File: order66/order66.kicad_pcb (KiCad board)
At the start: 2 copper layers, 232.6 x 124.3 mm, 144 parts, among them J1 NICEVIEW, J2 Pouch Battery Connector, SW1 AUX1, SW10 A, SW11 Z, SW12 AUX7, SW13 RST, SW14 2, SW15 W, SW16 S, SW17 X, SW18 LALT, SW19 ON/OFF, SW2 ESC, SW20 3, SW21 E, SW22 D, SW23 C, SW24 GUI, SW25 AUX5, SW26 4, SW27 R, SW28 F, SW29 V, SW3 TAB, SW30 RAISE, SW31 AUX4, SW32 5, SW33 T, SW34 G, SW35 B, SW36 AUX3, SW37 AUX2, SW38 6, SW39 Y, SW4 CAPSLCK, SW40 H, SW41 N, SW42 RSPACE, SW44 7, SW45 U, SW46 J, SW47 M, SW48 LOWER, SW5 LSHIFT, SW50 8, SW51 I, SW52 K, SW53 ,<, SW54 LEFT, SW56 9, SW57 O, SW58 L, SW59 .>, SW6 LCTRL, SW60 DOWN, SW62 0, SW63 P, SW64 ;:, SW65 /?, SW66 UP, SW67 AUX6, SW68 BACKSPACE, SW69 BACKSLACH, SW7 LSPACE, SW70 ENTER, SW71 RSHIFT, SW72 RIGHT, SW8 1, SW9 Q, U1 NiceNano

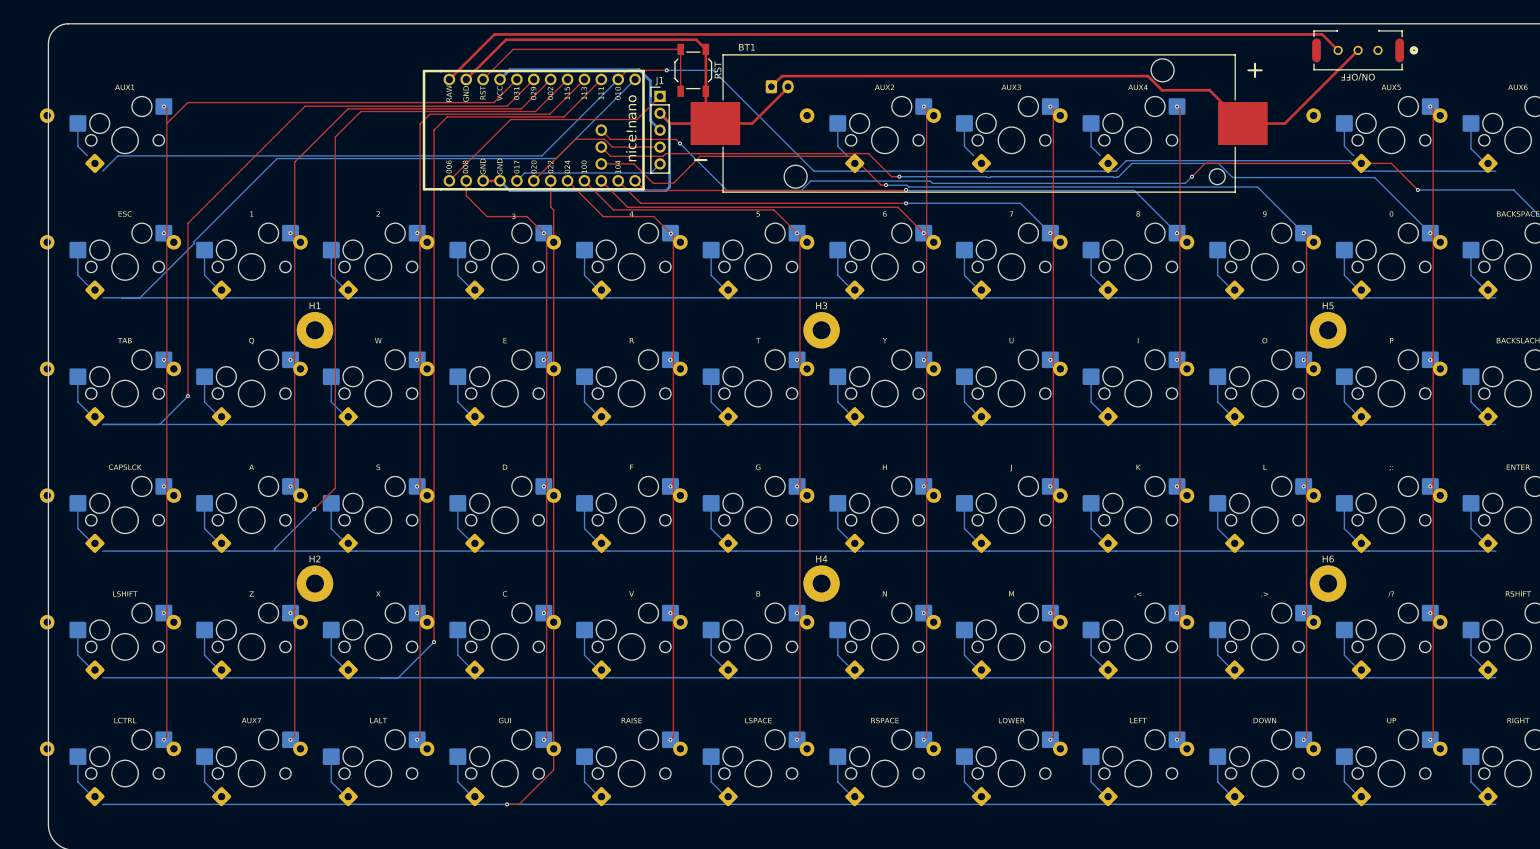
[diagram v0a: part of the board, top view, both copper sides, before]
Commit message: removing unused library files
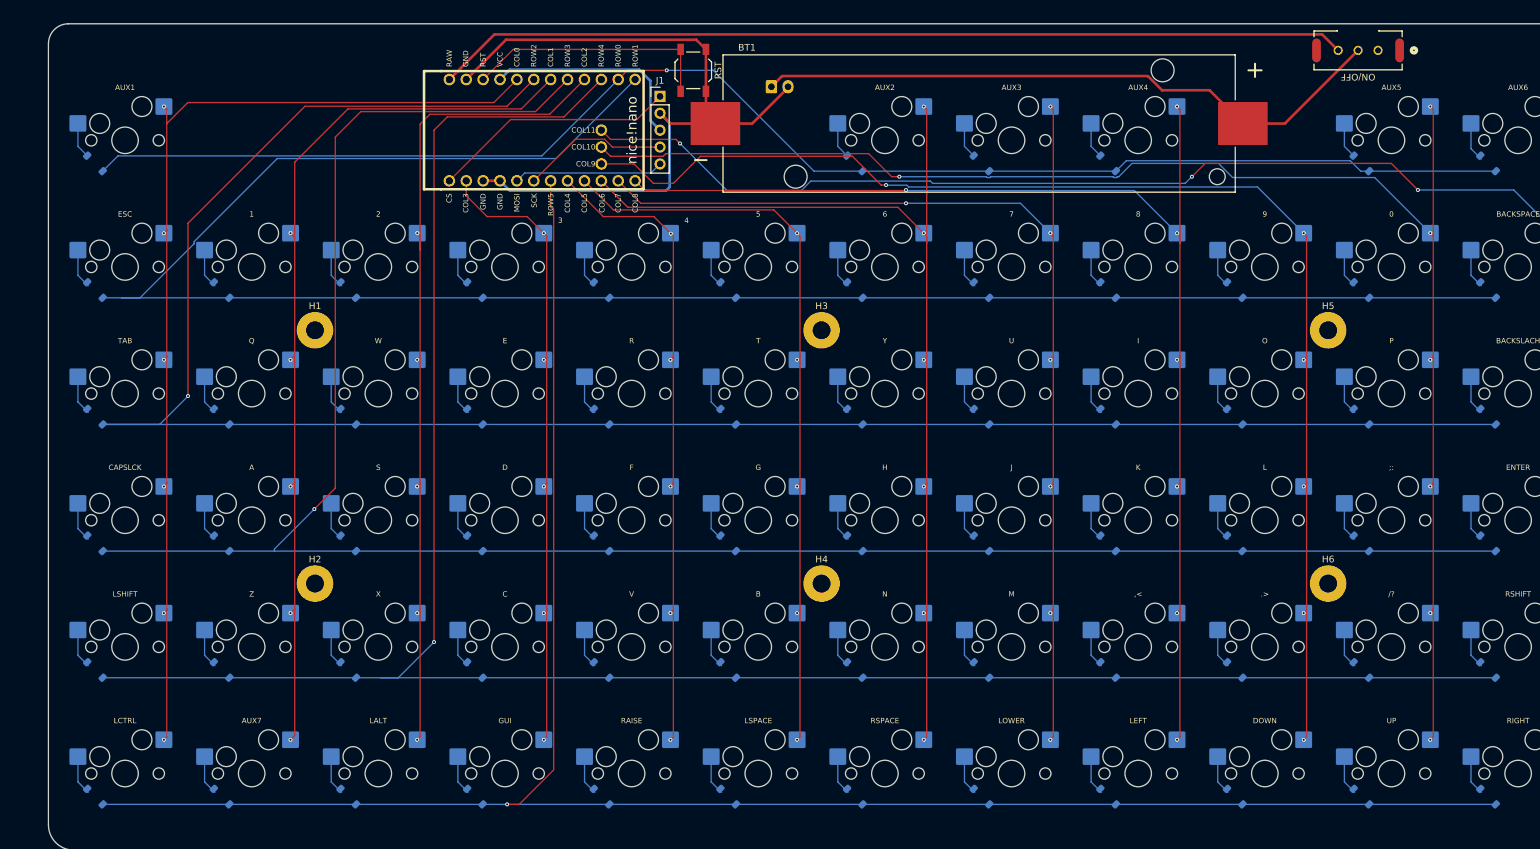
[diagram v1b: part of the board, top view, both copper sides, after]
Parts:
- D1, D10, D11, D12, D13, D14, D15, D16, D17, D18, D19, D2, D20, D21, D22, D23, D24, D25, D26, D27, D28, D29, D3, D30, D31, D32, D33, D34, D35, D38, D39, D4, D40, D41, D42, D44, D45, D46, D47, D48, D5, D50, D51, D52, D53, D54, D56, D57, D58, D59, D6, D60, D62, D63, D64, D65, D66, D67, D68, D69, D7, D70, D71, D72, D8, D9: footprint Diode_THT:D_DO-41_SOD81_P10.16mm_Horizontal -> Diode_SMD:D_SOD-123

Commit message: moved to more through hole components and rerouted traces
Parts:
- BT1: footprint 1042:BAT_1042 -> 1043P:BAT_1043P
- D1, D10, D11, D12, D13, D14, D15, D16, D17, D18, D19, D2, D20, D21, D22, D23, D24, D25, D26, D27, D28, D29, D3, D30, D31, D32, D33, D34, D35, D38, D39, D4, D40, D41, D42, D44, D45, D46, D47, D48, D5, D50, D51, D52, D53, D54, D56, D57, D58, D59, D6, D60, D62, D63, D64, D65, D66, D67, D68, D69, D7, D70, D71, D72, D8, D9: value 1N47xxA -> 1N4148; footprint Diode_SMD:D_SOD-123 -> Diode_THT:D_DO-35_SOD27_P7.62mm_Horizontal
- J2: footprint Connector_JST:JST_EH_S2B-EH_1x02_P2.50mm_Horizontal -> Connector_JST:JST_PH_B2B-PH-K_1x02_P2.00mm_Vertical
- SW13: footprint Button_Switch_SMD:SW_SPST_TL3342 -> Button_Switch_THT:SW_TH_Tactile_Omron_B3F-10xx
- moved SW13 92.5 mm to (276.0, 85.8), turned to 180 degrees
- moved D59 5.94 mm to (267.9, 166.4)
- moved D35 5.94 mm to (191.7, 166.4)
- moved D56 5.94 mm to (267.9, 109.2)
- moved D11 5.94 mm to (115.5, 166.4)
- moved D17 5.94 mm to (134.6, 166.4)
- moved D23 5.94 mm to (153.6, 166.4)
- moved D29 5.94 mm to (172.7, 166.4)
- moved D41 5.94 mm to (210.8, 166.4)
- moved D47 5.94 mm to (229.8, 166.4)
- moved D5 5.94 mm to (96.5, 166.4)
- moved D53 5.94 mm to (248.9, 166.4)
- moved D65 5.94 mm to (287.0, 166.4)
- moved D71 5.94 mm to (306.0, 166.4)
- moved D32 5.94 mm to (191.7, 109.2)
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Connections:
- U1 pad 11: COL7 -> COL9
- U1 pad 12: COL8 -> COL10
- U1 pad 13: ROW1 -> ROW2
- U1 pad 14: ROW0 -> ROW3
- U1 pad 17: ROW3 -> COL1
- U1 pad 18: COL1 -> ROW0
- U1 pad 19: ROW2 -> ROW1
- U1 pad 31: COL9 -> COL11
- U1 pad 32: COL10 -> COL7
- U1 pad 33: COL11 -> COL8
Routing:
- net GND: track 113.7 -> 231.5 mm
- net RST: track 37.9 -> 134.1 mm
- net ROW0: track 223.4 -> 244.0 mm, vias 1 -> 2
- net ROW2: track 311.1 -> 294.5 mm, vias 1 -> 0
- net ROW1: track 300.6 -> 309.6 mm
- net COL8: track 184.5 -> 193.4 mm, vias 7 -> 6
- net COL9: track 192.2 -> 185.3 mm, vias 6 -> 5
- net ROW3: track 314.1 -> 319.2 mm, vias 1 -> 0
- net COL10: track 230.8 -> 225.8 mm, vias 7 -> 6
- net VCC: track 31.9 -> 27.2 mm
- net ROW4: track 325.1 -> 329.7 mm, vias 1 -> 0
- net ROW5: track 307.5 -> 311.9 mm, vias 1 -> 0
- net COL7: track 166.9 -> 171.2 mm, vias 7 -> 6
- net COL1: track 135.4 -> 137.8 mm
- net BATT+: track 96.4 -> 94.3 mm
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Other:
- board size 232.6 x 124.3 mm -> 228.6 x 123 mm

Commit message: reordered the switch and diode numberings to be in order
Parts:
- renumbered D11 to D10, D12 to D11, D14 to D12, D15 to D13, D16 to D14, D17 to D15, D18 to D16, D20 to D17, D21 to D18, D22 to D19, D23 to D20, D24 to D21, D26 to D22, D27 to D23, D28 to D24, D29 to D25, D30 to D26, D32 to D27, D33 to D28, D34 to D29, D35 to D30, D7 to D31, D31 to D32, D38 to D33, D39 to D34, D40 to D35, D41 to D36, D42 to D37, D25 to D38, D44 to D39, D45 to D40, D46 to D41, D47 to D42, D48 to D43, D19 to D44, D50 to D45, D51 to D46, D52 to D47, D53 to D48, D54 to D49, D56 to D50, D57 to D51, D58 to D52, D59 to D53, D60 to D54, D13 to D55, D62 to D56, D63 to D57, D64 to D58, D65 to D59, D66 to D60, D67 to D61, D68 to D62, D69 to D63, D70 to D64, D71 to D65, D72 to D66, D8 to D7, D9 to D8, D10 to D9, SW11 to SW10, SW12 to SW11, SW14 to SW12, SW15 to SW13, SW16 to SW14, SW17 to SW15, SW18 to SW16, SW20 to SW17, SW21 to SW18, SW22 to SW19, SW23 to SW20, SW24 to SW21, SW26 to SW22, SW27 to SW23, SW28 to SW24, SW29 to SW25, SW30 to SW26, SW32 to SW27, SW33 to SW28, SW34 to SW29, SW35 to SW30, SW7 to SW31, SW37 to SW32, SW38 to SW33, SW39 to SW34, SW40 to SW35, SW41 to SW36, SW42 to SW37, SW36 to SW38, SW44 to SW39, SW45 to SW40, SW46 to SW41, SW47 to SW42, SW48 to SW43, SW31 to SW44, SW50 to SW45, SW51 to SW46, SW52 to SW47, SW53 to SW48, SW54 to SW49, SW56 to SW50, SW57 to SW51, SW58 to SW52, SW59 to SW53, SW60 to SW54, SW25 to SW55, SW62 to SW56, SW63 to SW57, SW64 to SW58, SW65 to SW59, SW66 to SW60, SW67 to SW61, SW68 to SW62, SW69 to SW63, SW70 to SW64, SW71 to SW65, SW72 to SW66, SW13 to SW67, SW19 to SW68, SW8 to SW7, SW9 to SW8, SW10 to SW9
